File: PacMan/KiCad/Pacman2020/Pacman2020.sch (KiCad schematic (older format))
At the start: 26 parts, among them J10 Conn_01x02, J11 Conn_01x02, J12 Conn_01x02, J13 Conn_01x14, J5 Conn_02x03_Odd_Even, J6 Conn_01x01, J7 Conn_01x01, J8 Conn_01x02, J9 Conn_01x02, Q2 DMN3404L, U1 R-785.0-1.0, U2 ATmega328P-AU

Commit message: update file names
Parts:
- removed J13: Conn_01x14, symbol Connector_Generic:Conn_01x14
- added J13: Conn_01x08, AERO_CUSTOM:TE_1-776280-1_8pin_Horizontal, symbol Connector_Generic:Conn_01x08
- D5: footprint (none) -> LED_SMD:LED_0603_1608Metric_Pad1.05x0.95mm_HandSolder
- F3: footprint (none) -> Fuse:Fuse_1812_4532Metric_Pad1.30x3.40mm_HandSolder
- H1, H2, H3, H4: footprint (none) -> MountingHole:MountingHole_3.2mm_M3
- J10, J11, J12, J9: footprint (none) -> Connector_JST:JST_VH_B2P-VH-B_1x02_P3.96mm_Vertical
- J5: footprint (none) -> Connector_PinHeader_2.00mm:PinHeader_2x03_P2.00mm_Vertical
- J6, J7: footprint (none) -> Connector_Hirose:Hirose_DF63R-1P-3.96DSA_1x01_P3.96mm_Vertical
- J8: footprint (none) -> Connector_Phoenix_MC_HighVoltage:PhoenixContact_MCV_1,5_2-GF-5.08_1x02_P5.08mm_Vertical_ThreadedFlange_MountHole
- Q2: footprint Package_TO_SOT_SMD:SOT-23 -> Package_TO_SOT_SMD:SOT-23_Handsoldering
- R4, R6: footprint (none) -> Resistor_SMD:R_0603_1608Metric_Pad0.98x0.95mm_HandSolder
- R5: footprint (none) -> Resistor_THT:R_Axial_DIN0617_L17.0mm_D6.0mm_P30.48mm_Horizontal
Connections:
- net labels added: 12_IN
- wire segments 82 -> 80
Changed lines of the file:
@@
 F4 "MAIN_CONT" I L 7525 5775 50
 $EndSheet
-$Comp
-L Connector_Generic:Conn_01x14 J13
-U 1 1 60073578
-P 10625 5375
-F 0 "J13" H 10705 5367 50  0000 L CNN
-F 1 "Conn_01x14" H 10705 5276 50  0000 L CNN
-F 2 "" H 10625 5375 50  0001 C CNN
-F 3 "~" H 10625 5375 50  0001 C CNN
-	1    10625 5375
-	1    0    0    -1
-$EndComp
 $Sheet
 S 5425 6900 1025 550
@@
 Wire Wire Line
 	5100 7025 5425 7025
-Text Label 10125 4775 0    50   ~ 0
+Text Label 10125 5275 0    50   ~ 0
 CAN+
 Wire Wire Line
-	10125 4775 10425 4775
-Text Label 10125 4875 0    50   ~ 0
+	10125 5275 10425 5275
+Text Label 10125 5375 0    50   ~ 0
 CAN-
 Wire Wire Line
-	10125 4875 10425 4875
-Text Label 10125 4975 0    50   ~ 0
-CAN+
-Wire Wire Line
-	10125 4975 10425 4975
-Text Label 10125 5075 0    50   ~ 0
-CAN-
-Wire Wire Line
-	10125 5075 10425 5075
+	10125 5375 10425 5375
 $Comp
 L power:+12V #PWR0104
 U 1 1 60080915
-P 9950 5175
-F 0 "#PWR0104" H 9950 5025 50  0001 C CNN
-F 1 "+12V" H 9965 5348 50  0000 C CNN
-F 2 "" H 9950 5175 50  0001 C CNN
-F 3 "" H 9950 5175 50  0001 C CNN
-	1    9950 5175
-	1    0    0    -1
-$EndComp
-Wire Wire Line
-	9950 5175 10425 5175
-Wire Wire Line
-	9950 5175 9950 5275
-Wire Wire Line
-	9950 5275 10425 5275
-Connection ~ 9950 5175
+P 9950 5475
+F 0 "#PWR0104" H 9950 5325 50  0001 C CNN
+F 1 "+12V" H 9965 5648 50  0000 C CNN
+F 2 "" H 9950 5475 50  0001 C CNN
+F 3 "" H 9950 5475 50  0001 C CNN
+	1    9950 5475
+	1    0    0    -1
+$EndComp
+Wire Wire Line
+	9950 5475 10425 5475
 $Comp
 L power:GND #PWR0105
@@
 $EndComp
 Wire Wire Line
-	9975 6075 10425 6075
-Wire Wire Line
 	10425 5975 9975 5975
 Wire Wire Line
 	9975 5975 9975 6075
-Connection ~ 9975 6075
 Wire Wire Line
 	4425 7225 4175 7225
@@
 F 0 "J5" H 3925 7442 50  0000 C CNN
 F 1 "Conn_02x03_Odd_Even" H 3925 7351 50  0000 C CNN
-F 2 "" H 3875 7125 50  0001 C CNN
+F 2 "Connector_PinHeader_2.00mm:PinHeader_2x03_P2.00mm_Vertical" H 3875 7125 50  0001 C CNN
 F 3 "~" H 3875 7125 50  0001 C CNN
 	1    3875 7125
@@
 F 0 "F3" V 850 6850 50  0000 C CNN
 F 1 "MF-MSMF050" V 925 6925 50  0000 C CNN
-F 2 "" H 1125 6650 50  0001 L CNN
+F 2 "Fuse:Fuse_1812_4532Metric_Pad1.30x3.40mm_HandSolder" H 1125 6650 50  0001 L CNN
 F 3 "~" H 1075 6850 50  0001 C CNN
 	1    1075 6850
@@
 F 0 "R4" V 2325 6875 50  0000 C CNN
 F 1 "330" V 2425 6850 50  0000 C CNN
-F 2 "" V 2355 6850 50  0001 C CNN
+F 2 "Resistor_SMD:R_0603_1608Metric_Pad0.98x0.95mm_HandSolder" V 2355 6850 50  0001 C CNN
 F 3 "~" H 2425 6850 50  0001 C CNN
 	1    2425 6850
@@
 F 0 "D5" H 2718 6595 50  0000 C CNN
 F 1 "LED" H 2718 6686 50  0000 C CNN
-F 2 "" H 2725 6850 50  0001 C CNN
+F 2 "LED_SMD:LED_0603_1608Metric_Pad1.05x0.95mm_HandSolder" H 2725 6850 50  0001 C CNN
 F 3 "~" H 2725 6850 50  0001 C CNN
 	1    2725 6850
@@
 	1    0    0    -1
 $EndComp
-Text Label 9875 5375 0    50   ~ 0
+Text Label 9875 5675 0    50   ~ 0
 PRECHARGE
 Wire Wire Line
-	9875 5375 10425 5375
-Text Label 9875 5475 0    50   ~ 0
+	9875 5675 10425 5675
+Text Label 9875 5775 0    50   ~ 0
 CONTACTOR
 Wire Wire Line
-	9875 5475 10425 5475
-Text Label 9875 5575 0    50   ~ 0
+	9875 5775 10425 5775
+Text Label 9875 5875 0    50   ~ 0
 SHUTDOWN_IN
 Wire Wire Line
-	9875 5575 10425 5575
+	9875 5875 10425 5875
 Text Label 6975 5675 0    50   ~ 0
 PRECHARGE
@@
 F 0 "H1" H 10375 746 50  0000 L CNN
 F 1 "MountingHole" H 10375 655 50  0000 L CNN
-F 2 "" H 10275 700 50  0001 C CNN
+F 2 "MountingHole:MountingHole_3.2mm_M3" H 10275 700 50  0001 C CNN
 F 3 "~" H 10275 700 50  0001 C CNN
 	1    10275 700
@@
 F 0 "Q2" H 8779 3321 50  0000 L CNN
 F 1 "DMN3404L" H 8779 3230 50  0000 L CNN
-F 2 "Package_TO_SOT_SMD:SOT-23" H 8775 3200 50  0001 L CIN
+F 2 "Package_TO_SOT_SMD:SOT-23_Handsoldering" H 8775 3200 50  0001 L CIN
 F 3 "http://www.diodes.com/assets/Datasheets/ds31787.pdf" H 8575 3275 50  0001 L CNN
 	1    8575 3275
@@
 F 0 "R6" H 8450 3500 50  0000 L CNN
 F 1 "10k" V 8375 3425 50  0000 L CNN
-F 2 "" V 8305 3500 50  0001 C CNN
+F 2 "Resistor_SMD:R_0603_1608Metric_Pad0.98x0.95mm_HandSolder" V 8305 3500 50  0001 C CNN
 F 3 "~" H 8375 3500 50  0001 C CNN
 	1    8375 3500
@@
 F 0 "J9" V 10775 2500 50  0000 R CNN
 F 1 "Conn_01x02" V 10700 2675 50  0000 R CNN
-F 2 "" H 10575 2525 50  0001 C CNN
+F 2 "Connector_JST:JST_VH_B2P-VH-B_1x02_P3.96mm_Vertical" H 10575 2525 50  0001 C CNN
 F 3 "~" H 10575 2525 50  0001 C CNN
 	1    10575 2525
@@
 F 0 "J10" V 10775 3025 50  0000 R CNN
 F 1 "Conn_01x02" V 10700 3200 50  0000 R CNN
-F 2 "" H 10575 3050 50  0001 C CNN
+F 2 "Connector_JST:JST_VH_B2P-VH-B_1x02_P3.96mm_Vertical" H 10575 3050 50  0001 C CNN
 F 3 "~" H 10575 3050 50  0001 C CNN
 	1    10575 3050
@@
 F 0 "J11" V 10775 3550 50  0000 R CNN
 F 1 "Conn_01x02" V 10700 3725 50  0000 R CNN
-F 2 "" H 10575 3575 50  0001 C CNN
+F 2 "Connector_JST:JST_VH_B2P-VH-B_1x02_P3.96mm_Vertical" H 10575 3575 50  0001 C CNN
 F 3 "~" H 10575 3575 50  0001 C CNN
 	1    10575 3575
@@
 F 0 "J12" V 10775 4050 50  0000 R CNN
 F 1 "Conn_01x02" V 10700 4225 50  0000 R CNN
-F 2 "" H 10575 4075 50  0001 C CNN
+F 2 "Connector_JST:JST_VH_B2P-VH-B_1x02_P3.96mm_Vertical" H 10575 4075 50  0001 C CNN
 F 3 "~" H 10575 4075 50  0001 C CNN
 	1    10575 4075
@@
 Connection ~ 10250 3675
 Wire Wire Line
-	10375 2525 10150 2525
-Wire Wire Line
-	10150 2525 10150 3050
+	10150 2300 10150 2525
 Wire Wire Line
 	10150 3050 10375 3050
@@
 Text Label 9175 3075 2    50   ~ 0
 FAN_OUT
-$Comp
-L power:+12V #PWR0117
-U 1 1 60142494
-P 10150 2375
-F 0 "#PWR0117" H 10150 2225 50  0001 C CNN
-F 1 "+12V" H 10165 2548 50  0000 C CNN
-F 2 "" H 10150 2375 50  0001 C CNN
-F 3 "" H 10150 2375 50  0001 C CNN
-	1    10150 2375
-	1    0    0    -1
-$EndComp
-Wire Wire Line
-	10150 2375 10150 2525
-Connection ~ 10150 2525
 Text Label 9875 4175 0    50   ~ 0
 FAN_OUT
@@
 F 0 "H2" H 10375 996 50  0000 L CNN
 F 1 "MountingHole" H 10375 905 50  0000 L CNN
-F 2 "" H 10275 950 50  0001 C CNN
+F 2 "MountingHole:MountingHole_3.2mm_M3" H 10275 950 50  0001 C CNN
 F 3 "~" H 10275 950 50  0001 C CNN
 	1    10275 950
@@
 F 0 "H3" H 10375 1246 50  0000 L CNN
 F 1 "MountingHole" H 10375 1155 50  0000 L CNN
-F 2 "" H 10275 1200 50  0001 C CNN
+F 2 "MountingHole:MountingHole_3.2mm_M3" H 10275 1200 50  0001 C CNN
 F 3 "~" H 10275 1200 50  0001 C CNN
 	1    10275 1200
@@
 F 0 "H4" H 10375 1496 50  0000 L CNN
 F 1 "MountingHole" H 10375 1405 50  0000 L CNN
-F 2 "" H 10275 1450 50  0001 C CNN
+F 2 "MountingHole:MountingHole_3.2mm_M3" H 10275 1450 50  0001 C CNN
 F 3 "~" H 10275 1450 50  0001 C CNN
 	1    10275 1450
@@
 F 0 "R5" H 5245 2046 50  0000 L CNN
 F 1 "39k" H 5245 1955 50  0000 L CNN
-F 2 "" V 5105 2000 50  0001 C CNN
+F 2 "Resistor_THT:R_Axial_DIN0617_L17.0mm_D6.0mm_P30.48mm_Horizontal" V 5105 2000 50  0001 C CNN
 F 3 "~" H 5175 2000 50  0001 C CNN
 	1    5175 2000
@@
 F 0 "J6" V 5139 1212 50  0000 R CNN
 F 1 "Conn_01x01" V 5048 1212 50  0000 R CNN
-F 2 "" H 5175 1300 50  0001 C CNN
+F 2 "Connector_Hirose:Hirose_DF63R-1P-3.96DSA_1x01_P3.96mm_Vertical" H 5175 1300 50  0001 C CNN
 F 3 "~" H 5175 1300 50  0001 C CNN
 	1    5175 1300
@@
 F 0 "J7" V 5047 2780 50  0000 L CNN
 F 1 "Conn_01x01" V 5138 2780 50  0000 L CNN
-F 2 "" H 5175 2700 50  0001 C CNN
+F 2 "Connector_Hirose:Hirose_DF63R-1P-3.96DSA_1x01_P3.96mm_Vertical" H 5175 2700 50  0001 C CNN
 F 3 "~" H 5175 2700 50  0001 C CNN
 	1    5175 2700
@@
 F 0 "J8" H 5780 2267 50  0000 L CNN
 F 1 "Conn_01x02" H 5780 2176 50  0000 L CNN
-F 2 "" H 5700 2275 50  0001 C CNN
+F 2 "Connector_Phoenix_MC_HighVoltage:PhoenixContact_MCV_1,5_2-GF-5.08_1x02_P5.08mm_Vertical_ThreadedFlange_MountHole" H 5700 2275 50  0001 C CNN
 F 3 "~" H 5700 2275 50  0001 C CNN
 	1    5700 2275
@@
 Wire Wire Line
 	5175 2375 5175 2500
+$Comp
+L Connector_Generic:Conn_01x08 J13
+U 1 1 600CA0BB
+P 10625 5575
+F 0 "J13" H 10705 5567 50  0000 L CNN
+F 1 "Conn_01x08" H 10705 5476 50  0000 L CNN
+F 2 "AERO_CUSTOM:TE_1-776280-1_8pin_Horizontal" H 10625 5575 50  0001 C CNN
+F 3 "~" H 10625 5575 50  0001 C CNN
+	1    10625 5575
+	1    0    0    -1
+$EndComp
+Wire Wire Line
+	9950 5575 10425 5575
+Wire Wire Line
+	9950 5575 9950 5475
+Connection ~ 9950 5475
+Text Label 1325 6850 0    50   ~ 0
+12_IN
+Text Label 10350 2300 2    50   ~ 0
+12_IN
+Wire Wire Line
+	10375 2525 10150 2525
+Connection ~ 10150 2525
+Wire Wire Line
+	10150 2525 10150 3050
+Wire Wire Line
+	10150 2300 10350 2300
 $EndSCHEMATC

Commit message: layout changes
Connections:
- net +12V: no longer J13.4 (Pin_4)
- net CONTACTOR: now also J13.4 (Pin_4); no longer J13.6 (Pin_6)
- net GND: now also J13.5 (Pin_5), J13.7 (Pin_7); no longer J13.8 (Pin_8)
- net PRECHARGE: now also J13.8 (Pin_8); no longer J13.5 (Pin_5)
- net SHUTDOWN_IN: now also J13.6 (Pin_6); no longer J13.7 (Pin_7)
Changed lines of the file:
@@
 L power:GND #PWR0105
 U 1 1 60081230
-P 9975 6075
-F 0 "#PWR0105" H 9975 5825 50  0001 C CNN
-F 1 "GND" H 9980 5902 50  0000 C CNN
-F 2 "" H 9975 6075 50  0001 C CNN
-F 3 "" H 9975 6075 50  0001 C CNN
-	1    9975 6075
-	1    0    0    -1
-$EndComp
-Wire Wire Line
-	10425 5975 9975 5975
-Wire Wire Line
-	9975 5975 9975 6075
+P 9725 5875
+F 0 "#PWR0105" H 9725 5625 50  0001 C CNN
+F 1 "GND" H 9730 5702 50  0000 C CNN
+F 2 "" H 9725 5875 50  0001 C CNN
+F 3 "" H 9725 5875 50  0001 C CNN
+	1    9725 5875
+	1    0    0    -1
+$EndComp
 Wire Wire Line
 	4425 7225 4175 7225
@@
 	1    0    0    -1
 $EndComp
-Text Label 9875 5675 0    50   ~ 0
+Text Label 9875 5975 0    50   ~ 0
 PRECHARGE
 Wire Wire Line
-	9875 5675 10425 5675
+	9875 5975 10425 5975
+Text Label 9875 5575 0    50   ~ 0
+CONTACTOR
+Wire Wire Line
+	9875 5575 10425 5575
 Text Label 9875 5775 0    50   ~ 0
-CONTACTOR
+SHUTDOWN_IN
 Wire Wire Line
 	9875 5775 10425 5775
-Text Label 9875 5875 0    50   ~ 0
-SHUTDOWN_IN
-Wire Wire Line
-	9875 5875 10425 5875
 Text Label 6975 5675 0    50   ~ 0
 PRECHARGE
@@
 	1    0    0    -1
 $EndComp
-Wire Wire Line
-	9950 5575 10425 5575
-Wire Wire Line
-	9950 5575 9950 5475
-Connection ~ 9950 5475
 Text Label 1325 6850 0    50   ~ 0
 12_IN
@@
 Wire Wire Line
 	10150 2300 10350 2300
+Wire Wire Line
+	9725 5675 10425 5675
+Wire Wire Line
+	9725 5875 10425 5875
+Wire Wire Line
+	9725 5675 9725 5875
+Connection ~ 9725 5875
 $EndSCHEMATC

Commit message: notes from design review 1
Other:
- note added: "TODO: \nWhat the hell are we doing? \nMake this thing better!!\nAlso, do the layout, pretty please"
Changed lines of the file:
@@
 	9725 5675 9725 5875
 Connection ~ 9725 5875
+Text Notes 4825 4425 0    126  ~ 0
+TODO: \nWhat the hell are we doing? \nMake this thing better!!\nAlso, do the layout, pretty please
 $EndSCHEMATC

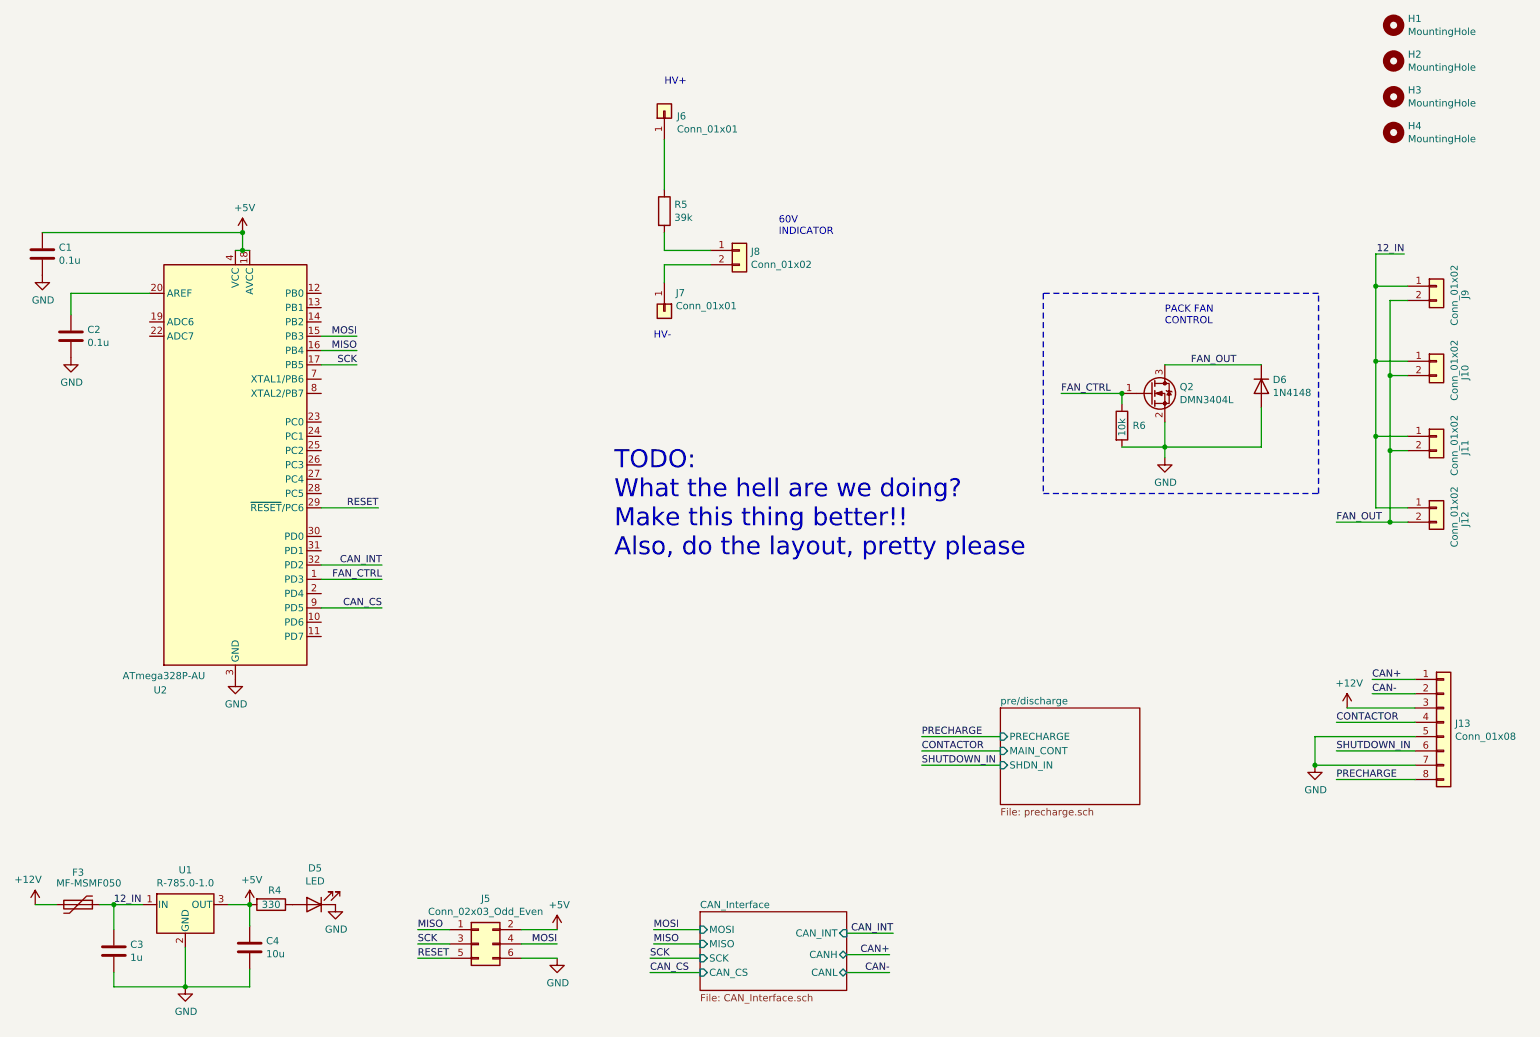
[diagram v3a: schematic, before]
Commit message: remove ATMEGA, add BMS fan control
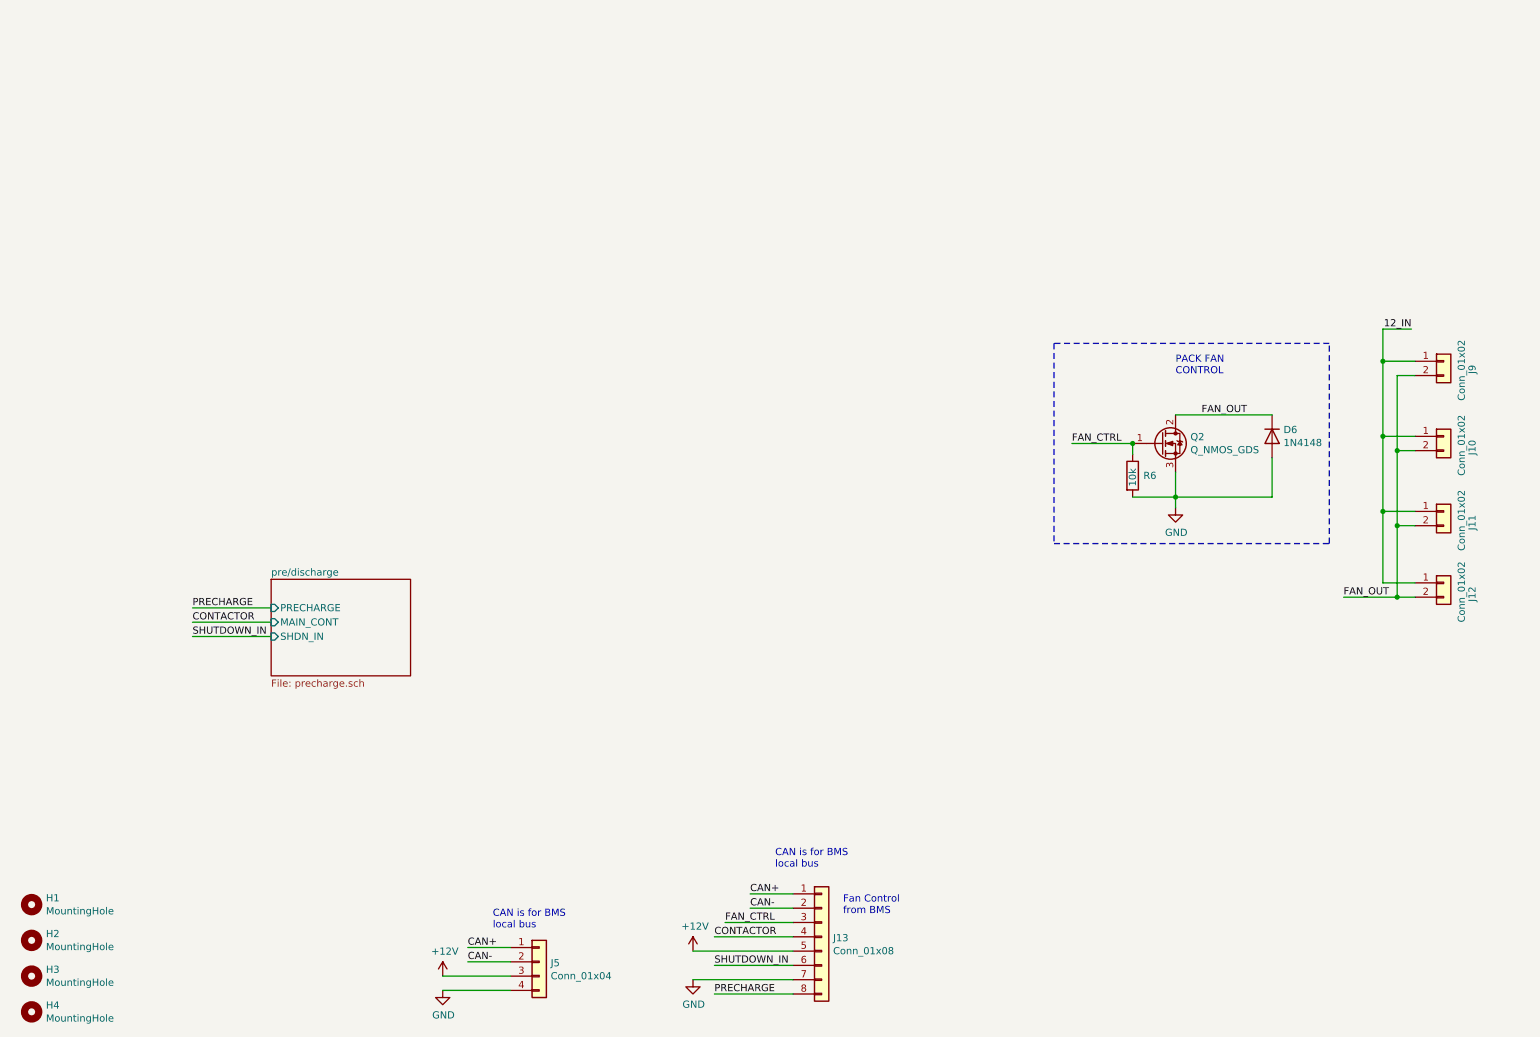
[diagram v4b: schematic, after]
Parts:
- removed C1, C2: 0.1u, Capacitor_SMD:C_0603_1608Metric_Pad1.08x0.95mm_HandSolder, symbol Device:C
- removed C3: 1u, Capacitor_SMD:C_0603_1608Metric_Pad1.08x0.95mm_HandSolder, symbol Device:C
- removed C4: 10u, Capacitor_SMD:C_0603_1608Metric_Pad1.08x0.95mm_HandSolder, symbol Device:C
- removed D5: LED, LED_SMD:LED_0603_1608Metric_Pad1.05x0.95mm_HandSolder, symbol Device:LED
- removed F3: MF-MSMF050, Fuse:Fuse_1812_4532Metric_Pad1.30x3.40mm_HandSolder, symbol Device:Polyfuse
- removed J5: Conn_02x03_Odd_Even, Connector_PinHeader_2.00mm:PinHeader_2x03_P2.00mm_Vertical, symbol Connector_Generic:Conn_02x03_Odd_Even
- removed J6, J7: Conn_01x01, Connector_Hirose:Hirose_DF63R-1P-3.96DSA_1x01_P3.96mm_Vertical, symbol Connector_Generic:Conn_01x01
- removed J8: Conn_01x02, Connector_Phoenix_MC_HighVoltage:PhoenixContact_MCV_1,5_2-GF-5.08_1x02_P5.08mm_Vertical_ThreadedFlange_MountHole, symbol Connector_Generic:Conn_01x02
- removed Q2: DMN3404L, Package_TO_SOT_SMD:SOT-23_Handsoldering, symbol Transistor_FET:DMN3404L
- removed R4: 330, Resistor_SMD:R_0603_1608Metric_Pad0.98x0.95mm_HandSolder, symbol Device:R
- removed R5: 39k, Resistor_THT:R_Axial_DIN0617_L17.0mm_D6.0mm_P30.48mm_Horizontal, symbol Device:R
- removed U1: R-785.0-1.0, Converter_DCDC:Converter_DCDC_RECOM_R-78E-0.5_THT, symbol Regulator_Switching:R-785.0-1.0
- removed U2: ATmega328P-AU, Package_QFP:TQFP-32_7x7mm_P0.8mm, symbol MCU_Microchip_ATmega:ATmega328P-AU
- added J5: Conn_01x04, Connector_JST:JST_PH_B4B-PH-K_1x04_P2.00mm_Vertical, symbol Connector_Generic:Conn_01x04
- added Q2: Q_NMOS_GDS, Package_TO_SOT_SMD:TO-252-3_TabPin2, symbol Device:Q_NMOS_GDS
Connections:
- net +12V: now also J13.5 (Pin_5), J5.3 (Pin_3); no longer J13.3 (Pin_3)
- net CAN+: now also J5.1 (Pin_1)
- net CAN-: now also J5.2 (Pin_2)
- net FAN_CTRL: now also J13.3 (Pin_3), Q2.1 (G)
- net FAN_OUT: now also Q2.2 (D)
- net GND: now also J5.4 (Pin_4), Q2.3 (S); no longer J13.5 (Pin_5)
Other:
- note added: "CAN is for BMS \nlocal bus\n"
- note added: "Fan Control \nfrom BMS"
- note removed: "60V \nINDICATOR\n"
- note removed: "HV+\n"
- note removed: "HV-\n"
- note removed: "TODO: \nWhat the hell are we doing? \nMake this thing better!!\nAlso, do the layout, pretty please"
- moved on the sheet: D6, H1, H2, H3, H4, J10, J11, J12, J13, J9, R6
